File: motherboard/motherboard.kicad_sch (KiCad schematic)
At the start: 21 parts, among them J1 532610471, J2 GSB1C41110SSHR, J3 532610471, J4 532610471, J5 532610471, J6 Conn_01x04_Pin, U1 RP2040, U2 ESP32-C3-WROOM-02U, U3 USBLC6-2SC6, U4 AP2112K-3.3TRG1

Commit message: fix : change composant
for next day :
- fix molex connector
- fix esp32 routing
- set pcb design
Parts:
- removed J6: Conn_01x04_Pin, Connector_PinHeader_1.00mm:PinHeader_1x04_P1.00mm_Vertical, symbol Connector:Conn_01x04_Pin
- removed U1: RP2040, Package_DFN_QFN:QFN-56-1EP_7x7mm_P0.4mm_EP3.2x3.2mm, symbol MCU_RaspberryPi:RP2040
- removed U3: USBLC6-2SC6, Package_TO_SOT_SMD:SOT-23-6, symbol Power_Protection:USBLC6-2SC6
- added J6, J7: 532610471, Library:MOLEX_532610471, symbol Connector_Header Surface Mount, Right Angle 4 position 0.049{dblquote} (1.25mm)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
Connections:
- net D+: now also U2.14 (IO19)
- net D-: now also U2.13 (IO18)
- net +3.3V: now reaches F1.1, U2.1 (3V3)
- net RX: no longer names the net of U2.12 (IO21/TXD)
- net TX: no longer names the net of U2.11 (IO20/RXD)
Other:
- company: (none) -> Modul X
- title: (none) -> Mother board Modul X
- moved on the sheet: C4, J1, J3, J4, J5, R3, U2, XTAL1

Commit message: update schema
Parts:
- added C5: 0.1µF, Capacitor_SMD:C_0201_0603Metric, symbol Device:C_Polarized
- added R6: 10 kΩ, Resistor_SMD:R_0201_0603Metric, symbol Device:R
- added SW1: SW_Push, symbol Switch:SW_Push
- C3: value 100nF -> 1µF
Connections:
- net +3.3V: now also C1.1, C2.1, R6.1
- net GND: now also C5.2, SW1.1
- net at J2.A4_B9 (VBUS_A), J2.B4_A9 (VBUS_B), U4.1 (VIN): now also U4.3 (EN); no longer C1.1, C2.1, C3.2
- net at F1.2, U4.5 (VOUT): now also C5.1
- net at U2.2 (EN): now also C3.2, R6.2, SW1.2
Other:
- moved on the sheet: C1, C2, U4

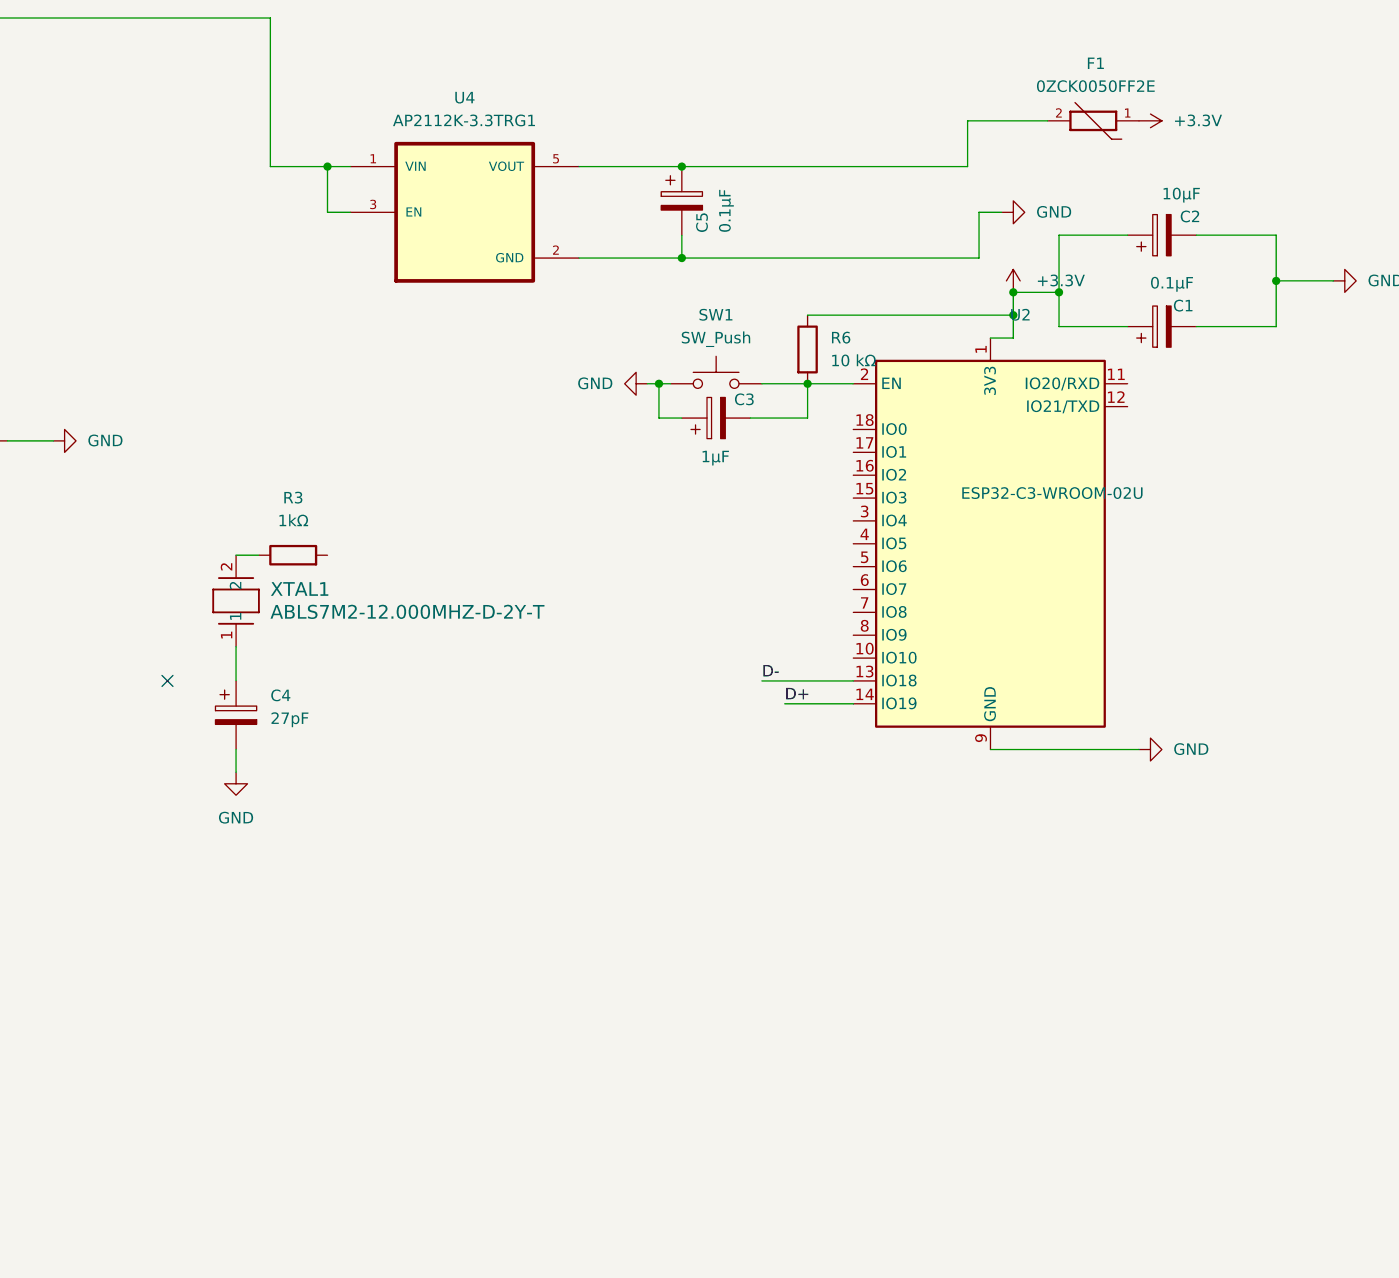
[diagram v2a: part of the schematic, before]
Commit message: fix : add connector i2c + button boot & reset
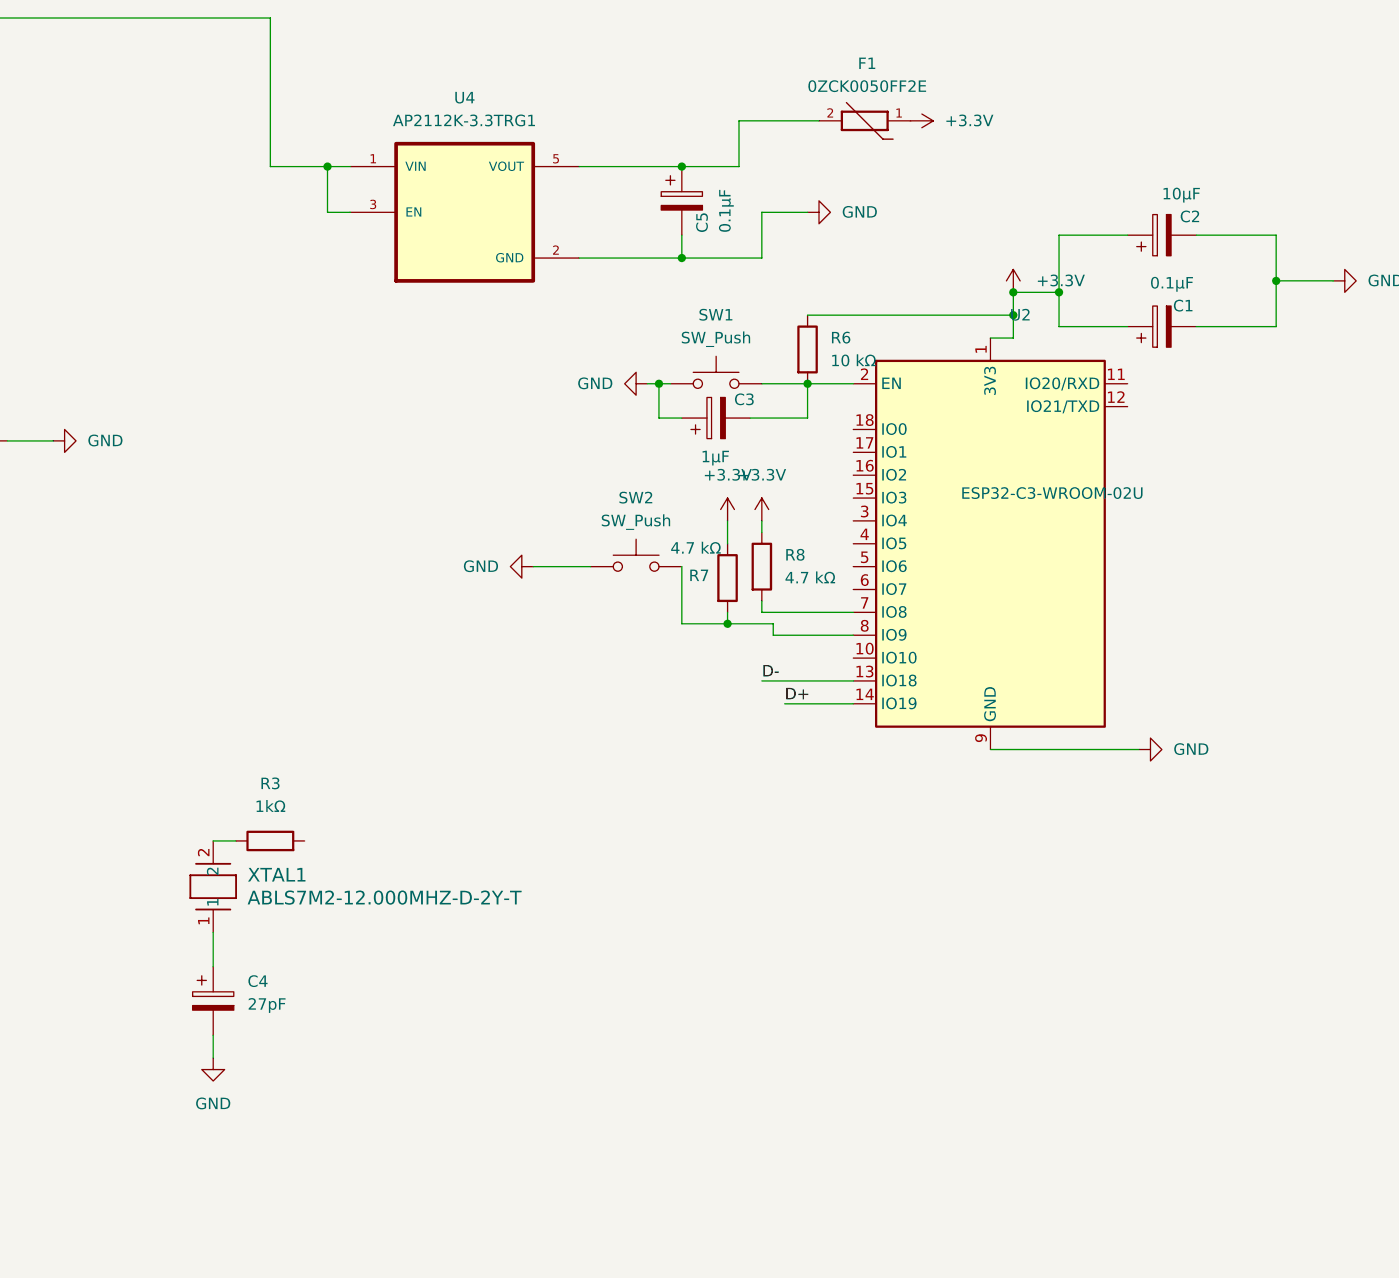
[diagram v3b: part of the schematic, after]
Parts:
- added R7, R8: 4.7 kΩ, Resistor_SMD:R_0201_0603Metric, symbol Device:R
- added SW2: SW_Push, symbol Switch:SW_Push
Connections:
- net +3.3V: now also R7.1, R8.1
- net GND: now also SW2.1
- net at U2.7 (IO8): now also R8.2
- net at U2.8 (IO9): now also R7.2, SW2.2
- no-connect marks 1 -> 0
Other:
- moved on the sheet: C4, F1, R3, XTAL1

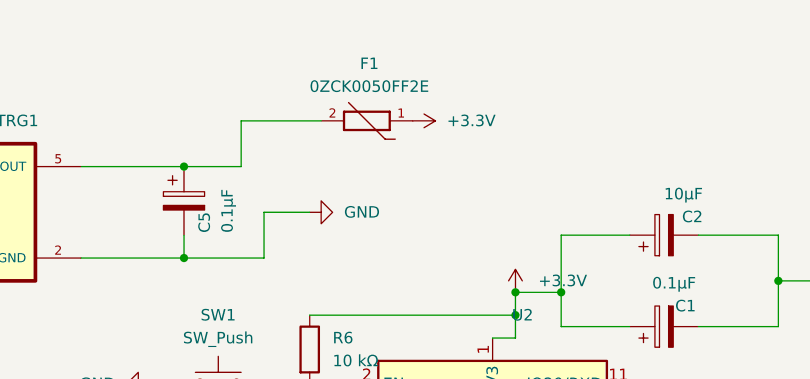
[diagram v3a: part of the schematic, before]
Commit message: fix : delete fusible (danger for esp32)
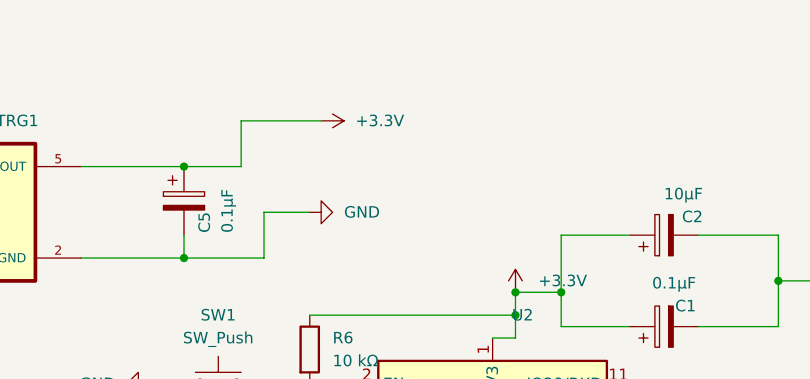
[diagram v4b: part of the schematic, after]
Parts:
- removed F1: 0ZCK0050FF2E, Library:FUSC2113X125N, symbol 0ZCK0050FF2E:0ZCK0050FF2E
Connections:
- net +3.3V: now also C5.1, U4.5 (VOUT)
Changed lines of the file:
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@@
 	(symbol
 		(lib_id "power:+3.3V")
-		(at 193.04 48.26 270)
+		(at 182.88 48.26 270)
 		(unit 1)
 		(exclude_from_sim no)
@@
 		(fields_autoplaced yes)
 		(property "Reference" "#PWR05"
-			(at 189.23 48.26 0)
+			(at 179.07 48.26 0)
 			(effects
 				(font
@@
 		)
 		(property "Value" "+3.3V"
-			(at 196.85 48.2599 90)
+			(at 186.69 48.2599 90)
 			(effects
 				(font
@@
 		)
 		(property "Footprint" ""
-			(at 193.04 48.26 0)
+			(at 182.88 48.26 0)
 			(effects
 				(font
@@
 		)
 		(property "Datasheet" ""
-			(at 193.04 48.26 0)
+			(at 182.88 48.26 0)
 			(effects
 				(font
@@
 		)
 		(property "Description" "Power symbol creates a global label with name \"+3.3V\""
-			(at 193.04 48.26 0)
+			(at 182.88 48.26 0)
 			(effects
 				(font
@@
 					(unit 1)
 				)
-			)
-		)
-	)
-	(symbol
-		(lib_id "0ZCK0050FF2E:0ZCK0050FF2E")
-		(at 187.96 48.26 0)
-		(unit 1)
-		(exclude_from_sim no)
-		(in_bom yes)
-		(on_board yes)
-		(dnp no)
-		(property "Reference" "F1"
-			(at 188.2394 41.91 0)
-			(effects
-				(font
-					(size 1.27 1.27)
-				)
-			)
-		)
-		(property "Value" "0ZCK0050FF2E"
-			(at 188.2394 44.45 0)
-			(effects
-				(font
-					(size 1.27 1.27)
-				)
-			)
-		)
-		(property "Footprint" "Library:FUSC2113X125N"
-			(at 187.96 48.26 0)
-			(effects
-				(font
-					(size 1.27 1.27)
-				)
-				(justify bottom)
-				(hide yes)
-			)
-		)
-		(property "Datasheet" ""
-			(at 187.96 48.26 0)
-			(effects
-				(font
-					(size 1.27 1.27)
-				)
-				(hide yes)
-			)
-		)
-		(property "Description" ""
-			(at 187.96 48.26 0)
-			(effects
-				(font
-					(size 1.27 1.27)
-				)
-				(hide yes)
-			)
-		)
-		(property "MAXIMUM_PACKAGE_HEIGHT" "1.25mm"
-			(at 187.96 48.26 0)
-			(effects
-				(font
-					(size 1.27 1.27)
-				)
-				(justify bottom)
-				(hide yes)
-			)
-		)
-		(property "CREATOR" "ANA"
-			(at 187.96 48.26 0)
-			(effects
-				(font
-					(size 1.27 1.27)
-				)
-				(justify bottom)
-				(hide yes)
-			)
-		)
-		(property "STANDARD" "IPC-7351B"
-			(at 187.96 48.26 0)
-			(effects
-				(font
-					(size 1.27 1.27)
-				)
-				(justify bottom)
-				(hide yes)
-			)
-		)
-		(property "PARTREV" "Apr2023"
-			(at 187.96 48.26 0)
-			(effects
-				(font
-					(size 1.27 1.27)
-				)
-				(justify bottom)
-				(hide yes)
-			)
-		)
-		(property "VERIFIER" ""
-			(at 187.96 48.26 0)
-			(effects
-				(font
-					(size 1.27 1.27)
-				)
-				(justify bottom)
-				(hide yes)
-			)
-		)
-		(property "MANUFACTURER" "Bel Fuse Inc."
-			(at 187.96 48.26 0)
-			(effects
-				(font
-					(size 1.27 1.27)
-				)
-				(justify bottom)
-				(hide yes)
-			)
-		)
-		(pin "1"
-		)
-		(pin "2"
-		)
-		(instances
-			(project ""
-				(path "/79d1bdac-2a68-4f9f-9c6a-2c63ad02609b"
-					(reference "F1")
-					(unit 1)
-				)

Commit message: fix : 3d model and footprint
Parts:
- removed C4: 27pF, Capacitor_SMD:C_0201_0603Metric, symbol Device:C_Polarized
- removed J1, J3, J4, J5, J6, J7: 532610471, Library:MOLEX_532610471, symbol Connector_Header Surface Mount, Right Angle 4 position 0.049{dblquote} (1.25mm)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
- removed R3: 1kΩ, Resistor_SMD:R_0201_0603Metric, symbol Device:R
- removed XTAL1: ABLS7M2-12.000MHZ-D-2Y-T, XTAL_ABLS7M2_ABR, symbol 2025-12-03_08-58-17:ABLS7M2-12.000MHZ-D-2Y-T
- added J1, J3, J5, J6: 532610571, CONN_532610001-SD_05_MOL, symbol CONN_532610001-SD_05_MOL:532610571
- J2: footprint Library:AMPHENOL_GSB1C41110SSHR -> footprint:AMPHENOL_GSB1C41110SSHR
- SW1, SW2: footprint (none) -> Button_Switch_SMD:SW_SPST_PTS810
- U4: footprint Library:SOT95P285X140-5N -> footprint:SOT95P285X140-5N
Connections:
- net +3.3V: now also U2.4 (IO5), J1.4, J3.4, J5.4, J6.1, J6.4
- net GND: now also J1.5, J3.5, J5.5, J6.5
- net SCL: now reaches R7.2, SW2.2, U2.8 (IO9)
- net SCL: now also J3.3, J5.3
- net SDA: now reaches R8.2, U2.7 (IO8)
- net SDA: now also J3.2, J5.2
- net ADC_Y_2: now reaches U2.15 (IO3)
- net ADC_Y_2: now also J6.2
- net ADC_X_2: now reaches U2.16 (IO2)
- net ADC_X_2: now also J6.3
- net ADC_Y_1: now reaches U2.17 (IO1)
- net ADC_Y_1: now also J1.2
- net ADC_X_1: now reaches U2.18 (IO0)
- net ADC_X_1: now also J1.3
- net CLICK_1: now reaches U2.3 (IO4)
- net CLICK_1: now also J1.1
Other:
- moved on the sheet: C3, SW2
